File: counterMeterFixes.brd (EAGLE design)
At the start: 100 x 64.4 mm, 128 parts, among them IC1 74AC14D, IC2 REG1117, IC3 74AC74D, IC4 74HC151D, IC5 74AC390D, IC6 74HC595D, IC7 74HC595D, J1 COMMON, J2 U/I/R, J3 10A, J4 U/I/R, K1 G6K-2P-Y, K2 G6K-2P-Y, K3 G6K-2P-Y, K4 G6K-2P-Y, K5 G6K-2P-Y, T1 BC847, T10 BC847, T2 BC847, T3 BC847, T4 BC847, T5 BC857, T6 BC857, T7 BC857, T8 BC857, T9 BC857, U1 MAX9201, U2 74XX161, U3 SN74LVC2G157DCTR, U4 MAX871, U5 AD8638, U6 AD8539

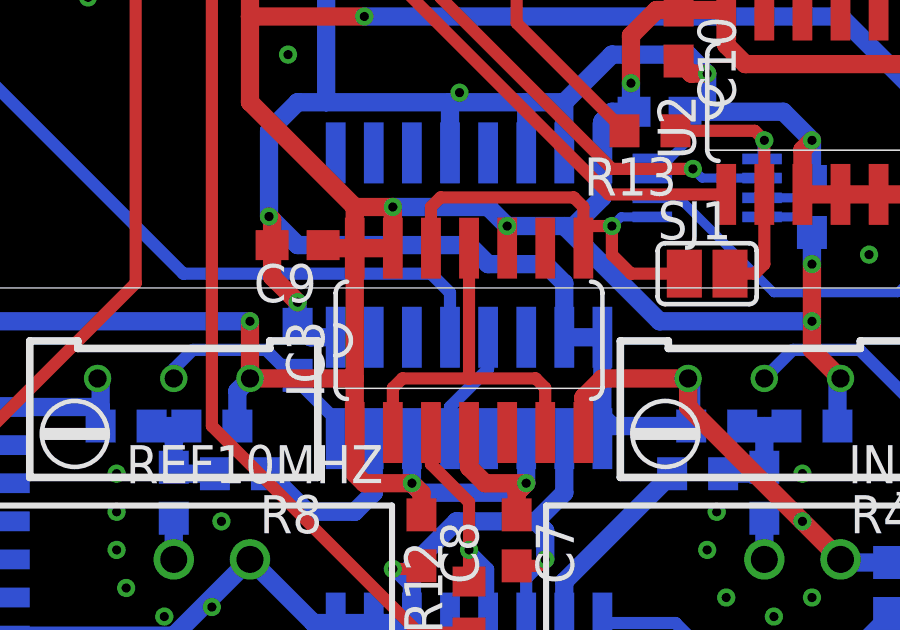
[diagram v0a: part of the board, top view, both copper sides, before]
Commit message: corrected frequency division of reference signal IC5A Pin 6 instead of 5
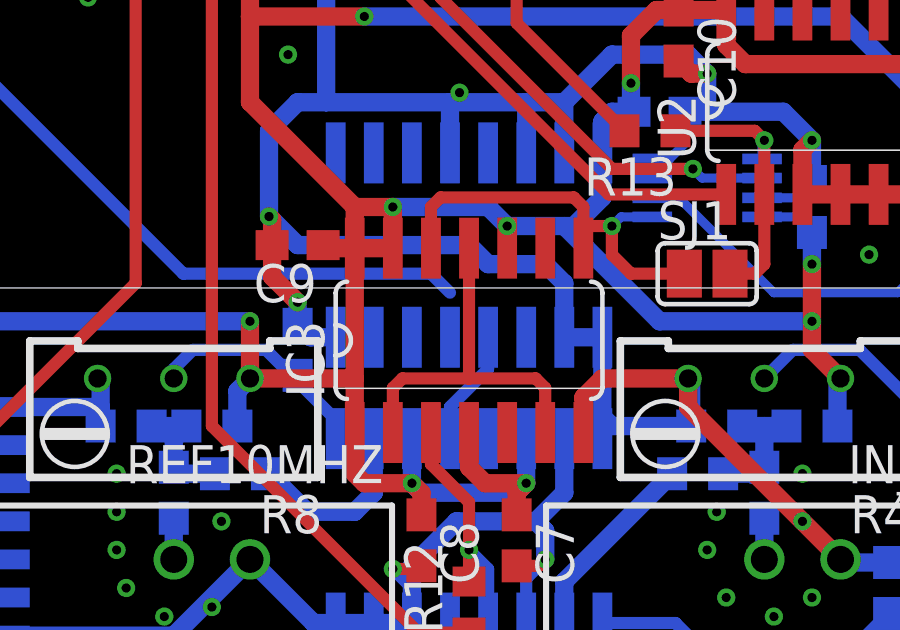
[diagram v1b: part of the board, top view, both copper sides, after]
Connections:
- net REF: now also IC5.6; no longer IC5.5
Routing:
- net REF: track 30.9 -> 29.4 mm
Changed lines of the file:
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@@
 </signal>
 <signal name="REF">
-<contactref element="IC5" pad="5"/>
 <contactref element="R60" pad="2"/>
-<wire x1="72.7075" y1="19.7866" x2="72.7075" y2="21.2725" width="0.4064" layer="16"/>
 <wire x1="72.7075" y1="21.2725" x2="72.0725" y2="21.9075" width="0.4064" layer="16"/>
 <wire x1="72.0725" y1="21.9075" x2="63.8175" y2="21.9075" width="0.4064" layer="16"/>
@@
 <wire x1="55.5625" y1="30.1625" x2="47.0925" y2="30.1625" width="0.4064" layer="16"/>
 <wire x1="47.0925" y1="30.1625" x2="46.99" y2="30.265" width="0.4064" layer="16"/>
+<contactref element="IC5" pad="6"/>
+<wire x1="72.7075" y1="21.2725" x2="71.4375" y2="19.7866" width="0" layer="19" extent="16-16"/>
 </signal>
 <signal name="I_10A">
